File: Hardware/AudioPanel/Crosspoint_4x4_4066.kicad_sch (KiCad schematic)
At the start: 11 parts, among them U91 4066, U92 4066, U93 4066

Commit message: Cleaned up stuff, defined more busses
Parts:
- renumbered C785 to C801, C786 to C802, C792 to C803, C791 to C804, C787 to C805, C789 to C806, C788 to C807, C790 to C808, U91 to U106, U92 to U107, U93 to U108

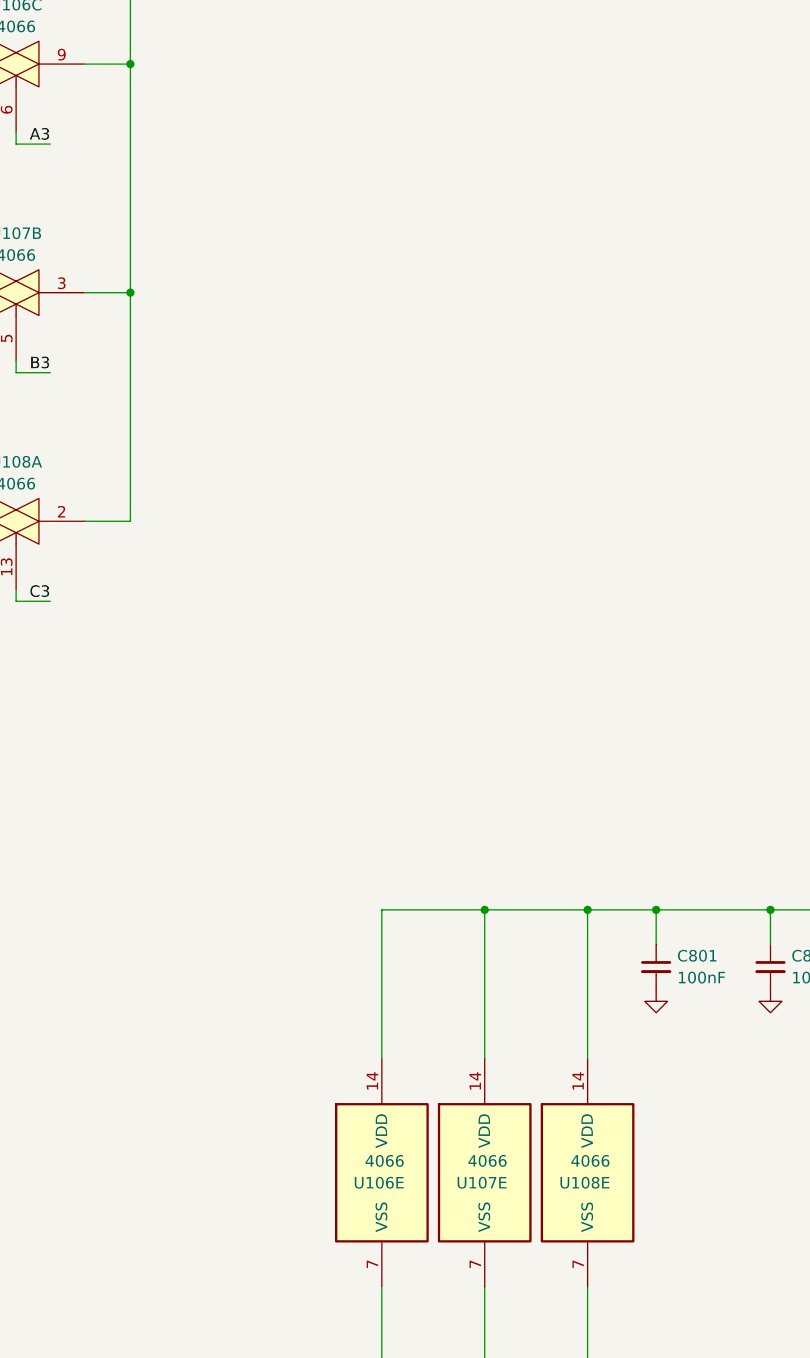
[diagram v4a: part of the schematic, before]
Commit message: Added speaker and headphone audio switching
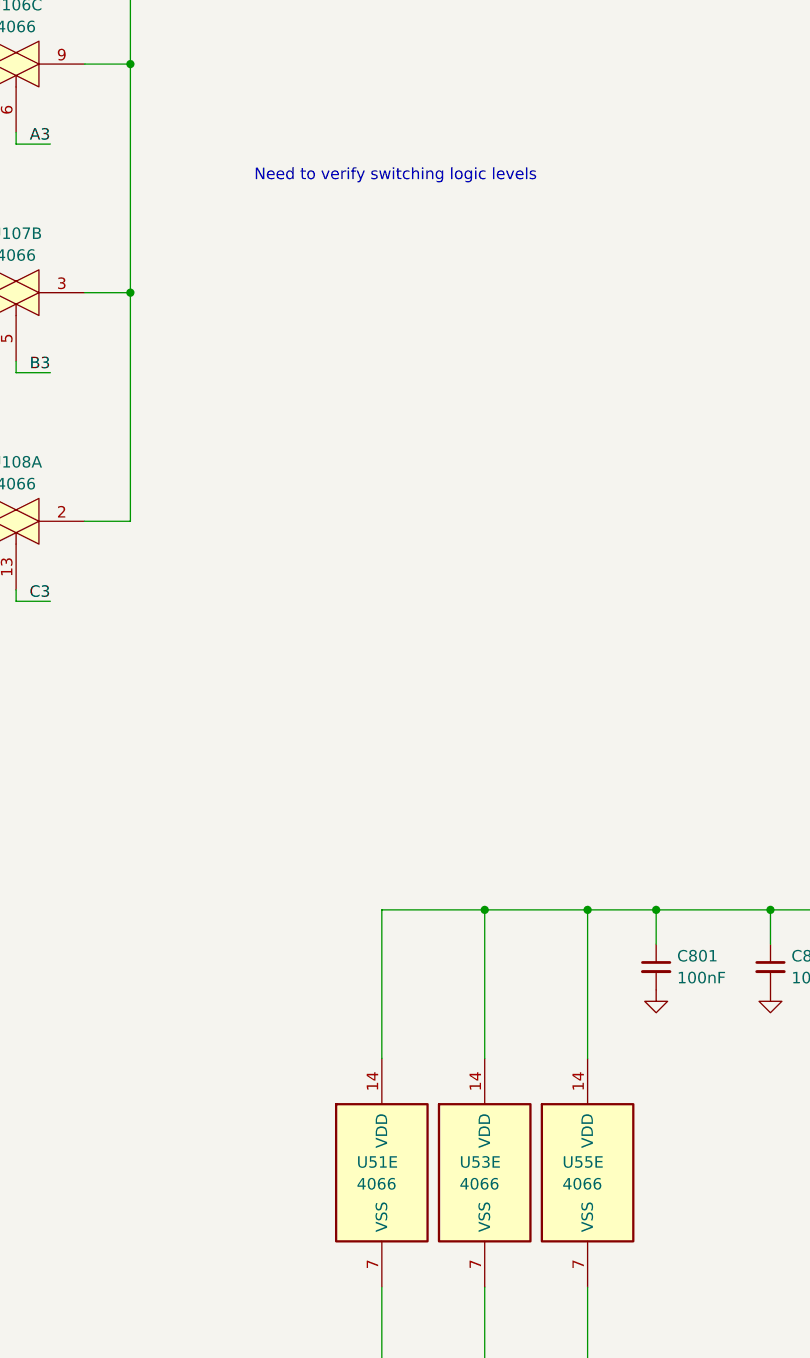
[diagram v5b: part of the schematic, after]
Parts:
- removed unit 5 of U106
- removed unit 5 of U107
- removed unit 5 of U108
- added U51, U53, U55: 4066, symbol 4xxx:4066
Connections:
- net VDD: now also U51.14 (VDD), U53.14 (VDD), U55.14 (VDD)
- net VSS: now also U51.7 (VSS), U53.7 (VSS), U55.7 (VSS)
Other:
- note added: "Need to verify switching logic levels"
